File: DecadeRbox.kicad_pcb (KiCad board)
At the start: 2 copper layers, 15.2 x 30.5 mm, 12 parts, among them J1 Conn_01x01, J2 Conn_01x11, J3 Conn_01x01

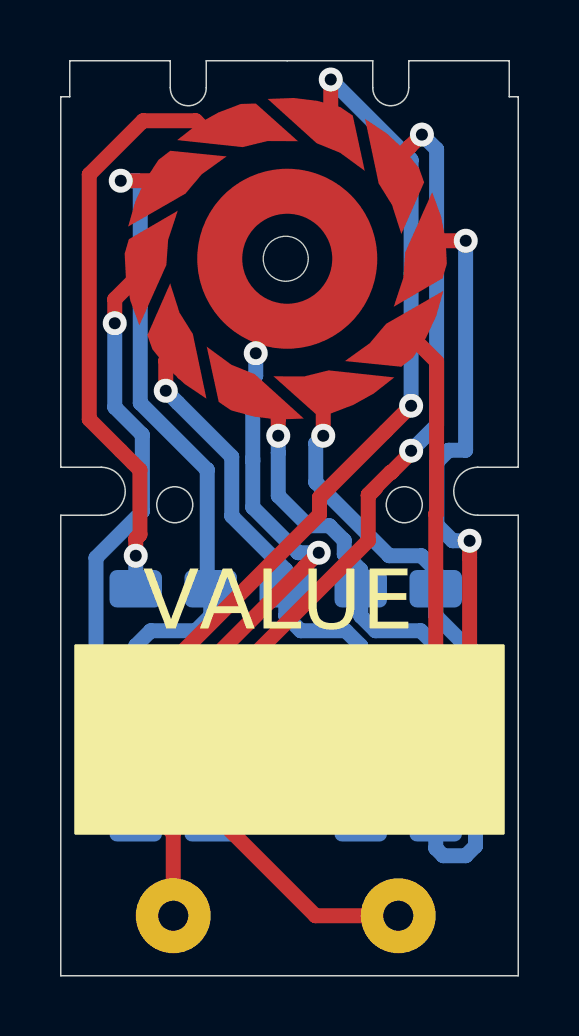
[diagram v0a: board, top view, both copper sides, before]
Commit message: Thicken some traces where possible
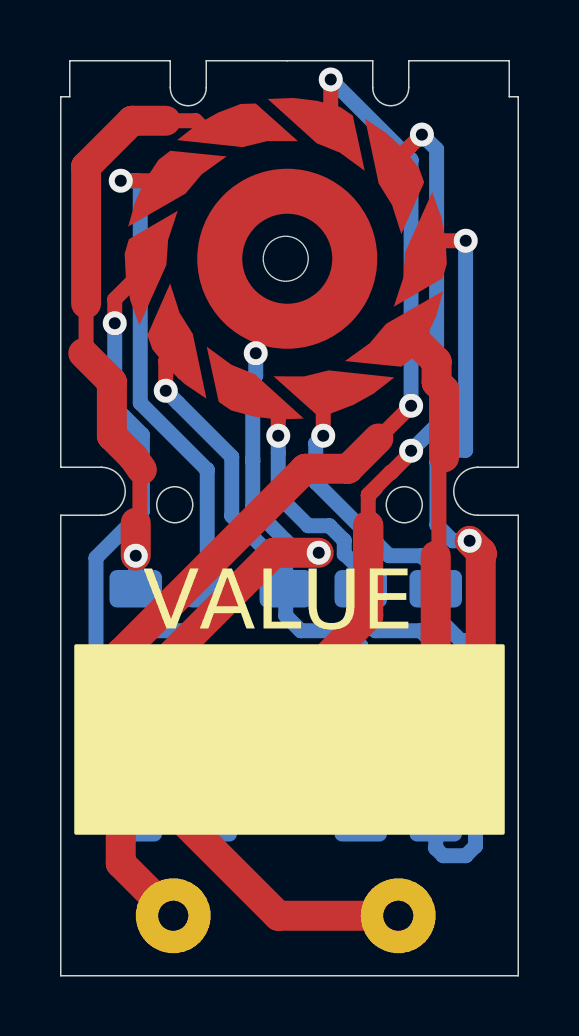
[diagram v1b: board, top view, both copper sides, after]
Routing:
- net Net-(J1-Pad1): track 28.1 -> 30.5 mm
- net Net-(J2-Pad9): track 30.9 -> 32.4 mm
- net Net-(J2-Pad10): track 30.9 -> 32.3 mm
- net Net-(J2-Pad8): track 19.0 -> 20.3 mm
- net Net-(J2-Pad11): track 37.8 -> 38.7 mm
